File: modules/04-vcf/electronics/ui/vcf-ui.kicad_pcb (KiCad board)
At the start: 2 copper layers, 58 x 110 mm, 46 parts, among them J1 Conn_02x03_Odd_Even, J2 Conn_02x02_Counter_Clockwise, J4 Conn_01x02, J5 Conn_01x06, J6 Conn_02x04_Odd_Even, U1 TL072

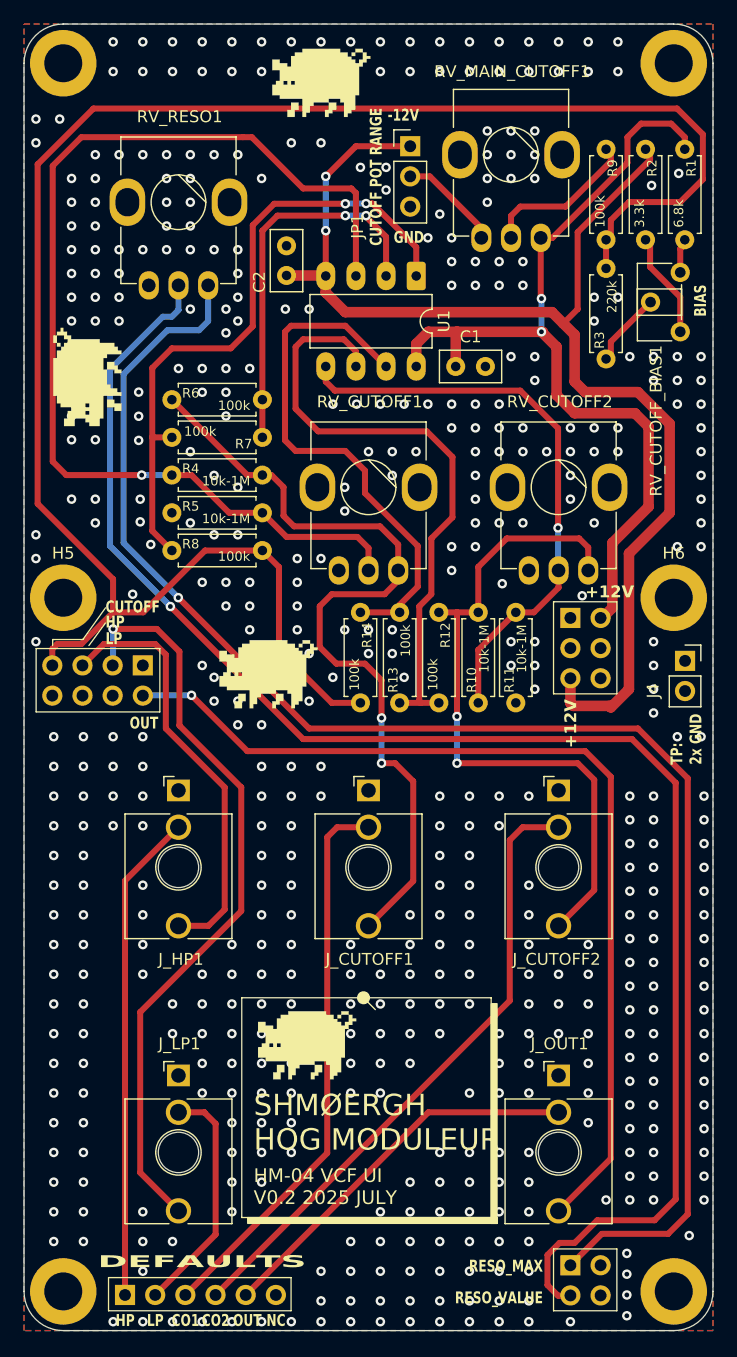
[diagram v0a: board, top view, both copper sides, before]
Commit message: Fixed VCF connector positions
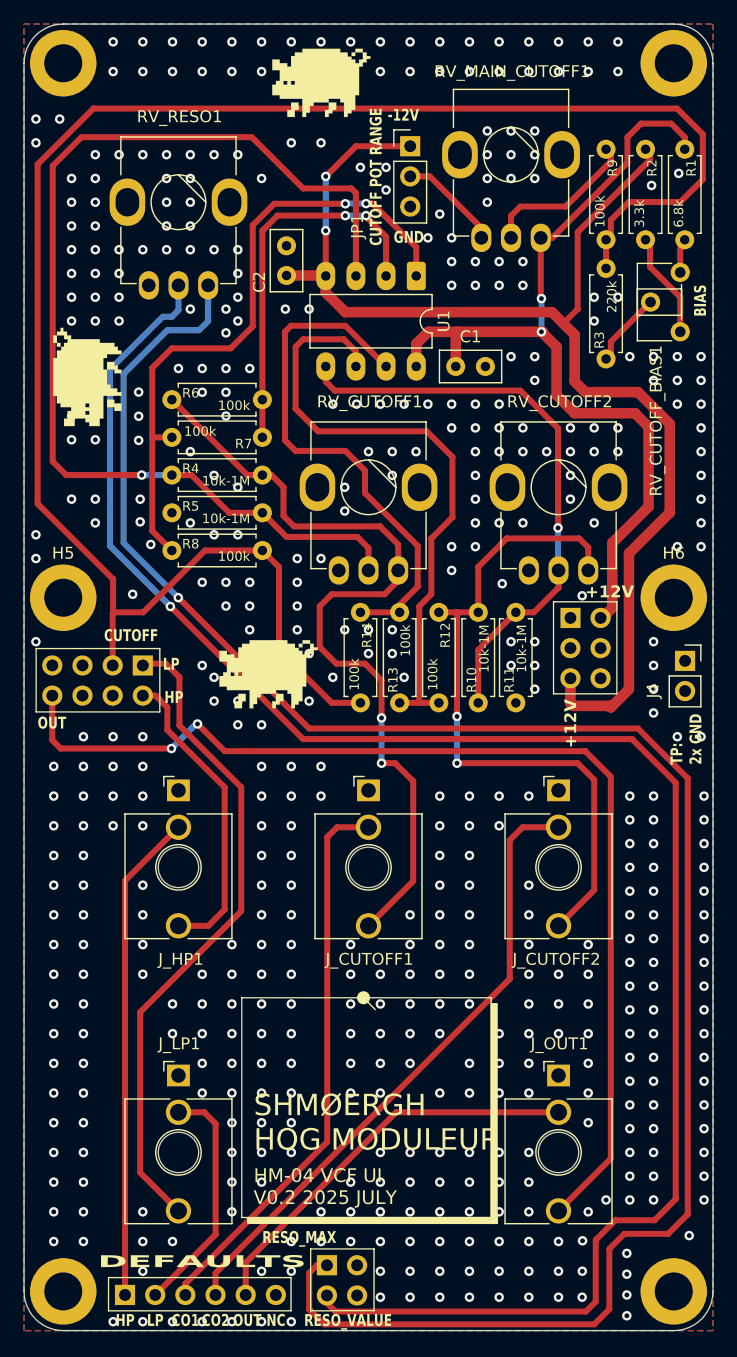
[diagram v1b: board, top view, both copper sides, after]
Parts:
- removed the G*** at (147.8, 130.0)
- C1, C2: value C -> 100n
- moved J2 20.5 mm to (149.5, 148.5)
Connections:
- J6 pad 1: unconnected-(J6-Pin_1-Pad1) -> LP_IN
- J6 pad 2: OUT -> HP_IN
- J6 pad 3: LP_IN -> CUTOFF
- J6 pad 5: HP_IN -> unconnected-(J6-Pin_5-Pad5)
- J6 pad 7: CUTOFF -> unconnected-(J6-Pin_7-Pad7)
- J6 pad 8: unconnected-(J6-Pin_8-Pad8) -> OUT
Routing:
- net RESO_MAX: track 130.3 -> 162.6 mm
- net RESO_VALUE: track 133.3 -> 153.0 mm
- net OUT: track 80.6 -> 92.1 mm, vias 1 -> 2
- net HP_IN: track 36.1 -> 26.0 mm
- net LP_IN: track 63.6 -> 55.6 mm, vias 1 -> 0
- net CUTOFF: track 156.6 -> 153.3 mm
- net OUT_DEFAULT: track 32.7 -> 34.3 mm
- net GND: vias 523 -> 528

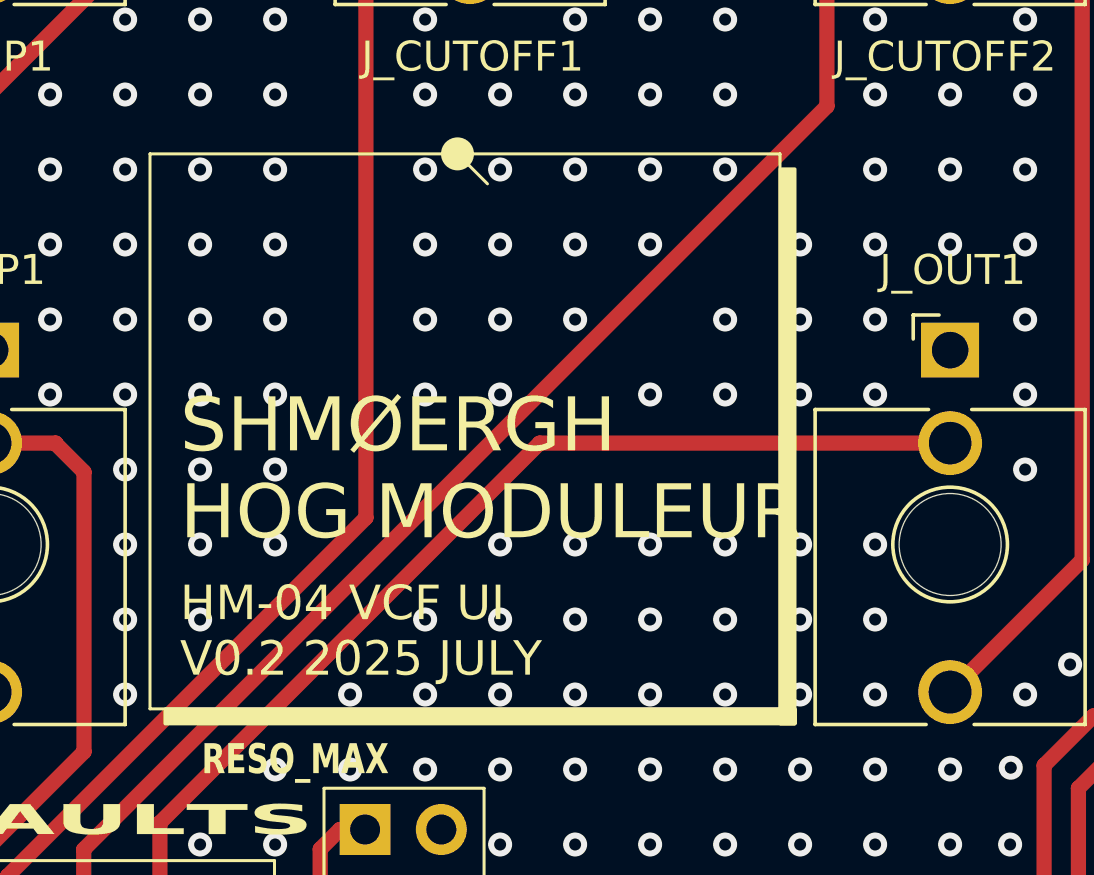
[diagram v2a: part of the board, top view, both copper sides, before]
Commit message: Updated text on PCB
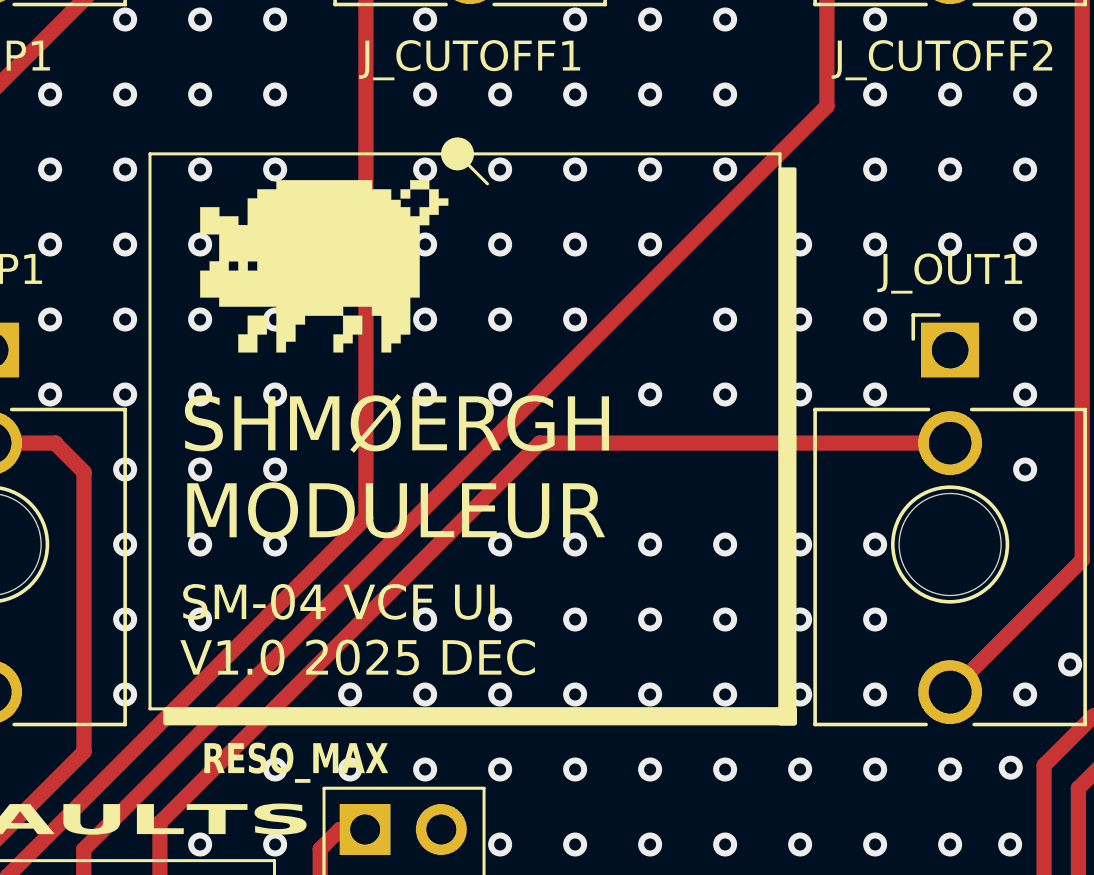
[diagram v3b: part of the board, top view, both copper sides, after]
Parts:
- added G***: LOGO, Shmoergh_Logo:Gyeszno, F.Cu at (148.1, 129.7)
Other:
- board text added: "SHMØERGH MODULEUR"
- board text added: "SM-04 VCF UI V1.0 2025 DEC"
- board text removed: "HM-04 VCF UI V0.2 2025 JULY"
- board text removed: "SHMØERGH HOG MODULEUR"

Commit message: KiCAD version update - VCF
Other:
- board text added: "SM-04 VCF UI V1.0"
- board text removed: "SM-04 VCF UI V1.0 2025 DEC"
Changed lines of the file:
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@@
 		)
 	)
-	(gr_text "SM-04 VCF UI \nV1.0 2025 DEC"
+	(gr_text "SM-04 VCF UI \nV1.0"
 		(at 143.329 143.479 0)
 		(layer "F.SilkS")
@@
 			(justify left bottom)
 		)
-		(render_cache "SM-04 VCF UI \nV1.0 2025 DEC" 0
+		(render_cache "SM-04 VCF UI \nV1.0" 0
 			(polygon
 				(pts
@@
 				)
 			)
-			(polygon
-				(pts
-					(xy 148.592958 142.990823) (xy 148.592958 143.2835) (xy 149.324789 143.2835) (xy 149.324789 143.137161)
-					(xy 148.739296 143.137161) (xy 148.739296 142.990823)
-				)
-			)
-			(polygon
-				(pts
-					(xy 149.178381 142.258992) (xy 149.178381 142.112584) (xy 148.739296 142.112584) (xy 148.739296 142.258992)
-				)
-			)
-			(polygon
-				(pts
-					(xy 149.178381 142.258992) (xy 149.178381 142.551739) (xy 149.324789 142.551739) (xy 149.324789 142.258992)
-				)
-			)
-			(polygon
-				(pts
-					(xy 148.739296 142.844415) (xy 148.739296 142.990823) (xy 148.885704 142.990823) (xy 148.885704 142.844415)
-				)
-			)
-			(polygon
-				(pts
-					(xy 148.592958 142.258992) (xy 148.592958 142.40533) (xy 148.739296 142.40533) (xy 148.739296 142.258992)
-				)
-			)
-			(polygon
-				(pts
-					(xy 149.032043 142.551739) (xy 149.032043 142.698077) (xy 149.178381 142.698077) (xy 149.178381 142.551739)
-				)
-			)
-			(polygon
-				(pts
-					(xy 148.885704 142.698077) (xy 148.885704 142.844415) (xy 149.032043 142.844415) (xy 149.032043 142.698077)
-				)
-			)
-			(polygon
-				(pts
-					(xy 149.616482 142.258992) (xy 149.616482 143.137161) (xy 149.76282 143.137161) (xy 149.76282 142.844415)
-					(xy 149.909228 142.844415) (xy 149.909228 142.698077) (xy 149.76282 142.698077) (xy 149.76282 142.258992)
-				)
-			)
-			(polygon
-				(pts
-					(xy 149.76282 143.137161) (xy 149.76282 143.2835) (xy 150.201905 143.2835) (xy 150.201905 143.137161)
-				)
-			)
-			(polygon
-				(pts
-					(xy 149.76282 142.112584) (xy 149.76282 142.258992) (xy 150.201905 142.258992) (xy 150.201905 142.112584)
-				)
-			)
-			(polygon
-				(pts
-					(xy 150.201905 142.258992) (xy 150.201905 142.40533) (xy 150.055567 142.40533) (xy 150.055567 142.551739)
-					(xy 150.201905 142.551739) (xy 150.201905 143.137161) (xy 150.348313 143.137161) (xy 150.348313 142.258992)
-				)
-			)
-			(polygon
-				(pts
-					(xy 149.909228 142.551739) (xy 149.909228 142.698077) (xy 150.055567 142.698077) (xy 150.055567 142.551739)
-				)
-			)
-			(polygon
-				(pts
-					(xy 150.640006 142.990823) (xy 150.640006 143.2835) (xy 151.371837 143.2835) (xy 151.371837 143.137161)
-					(xy 150.786344 143.137161) (xy 150.786344 142.990823)
-				)
-			)
-			(polygon
-				(pts
-					(xy 151.225429 142.258992) (xy 151.225429 142.112584) (xy 150.786344 142.112584) (xy 150.786344 142.258992)
-				)
-			)
-			(polygon
-				(pts
-					(xy 151.225429 142.258992) (xy 151.225429 142.551739) (xy 151.371837 142.551739) (xy 151.371837 142.258992)
-				)
-			)
-			(polygon
-				(pts
-					(xy 150.786344 142.844415) (xy 150.786344 142.990823) (xy 150.932753 142.990823) (xy 150.932753 142.844415)
-				)
-			)
-			(polygon
-				(pts
-					(xy 150.640006 142.258992) (xy 150.640006 142.40533) (xy 150.786344 142.40533) (xy 150.786344 142.258992)
-				)
-			)
-			(polygon
-				(pts
-					(xy 151.079091 142.551739) (xy 151.079091 142.698077) (xy 151.225429 142.698077) (xy 151.225429 142.551739)
-				)
-			)
-			(polygon
-				(pts
-					(xy 150.932753 142.698077) (xy 150.932753 142.844415) (xy 151.079091 142.844415) (xy 151.079091 142.698077)
-				)
-			)
-			(polygon
-				(pts
-					(xy 151.66353 142.112584) (xy 151.66353 142.698077) (xy 152.248953 142.698077) (xy 152.248953 142.551739)
-					(xy 151.809868 142.551739) (xy 151.809868 142.258992) (xy 152.395361 142.258992) (xy 152.395361 142.112584)
-				)
-			)
-			(polygon
-				(pts
-					(xy 152.248953 142.698077) (xy 152.248953 143.137161) (xy 152.395361 143.137161) (xy 152.395361 142.698077)
-				)
-			)
-			(polygon
-				(pts
-					(xy 152.248953 143.137161) (xy 151.809868 143.137161) (xy 151.809868 143.2835) (xy 152.248953 143.2835)
-				)
-			)
-			(polygon
-				(pts
-					(xy 151.809868 143.137161) (xy 151.809868 142.990823) (xy 151.66353 142.990823) (xy 151.66353 143.137161)
-				)
-			)
-			(polygon
-				(pts
-					(xy 153.710578 142.112584) (xy 153.710578 143.2835) (xy 154.296001 143.2835) (xy 154.296001 143.137161)
-					(xy 153.856916 143.137161) (xy 153.856916 142.258992) (xy 154.296001 142.258992) (xy 154.296001 142.112584)
-				)
-			)
-			(polygon
-				(pts
-					(xy 154.296001 142.258992) (xy 154.296001 143.137161) (xy 154.442409 143.137161) (xy 154.442409 142.258992)
-				)
-			)
-			(polygon
-				(pts
-					(xy 154.734102 142.112584) (xy 154.734102 143.2835) (xy 155.465933 143.2835) (xy 155.465933 143.137161)
-					(xy 154.880441 143.137161) (xy 154.880441 142.698077) (xy 155.319525 142.698077) (xy 155.319525 142.551739)
-					(xy 154.880441 142.551739) (xy 154.880441 142.258992) (xy 155.465933 142.258992) (xy 155.465933 142.112584)
-				)
-			)
-			(polygon
-				(pts
-					(xy 155.757627 142.258992) (xy 155.757627 143.137161) (xy 155.903965 143.137161) (xy 155.903965 142.258992)
-				)
-			)
-			(polygon
-				(pts
-					(xy 155.903965 143.137161) (xy 155.903965 143.2835) (xy 156.343049 143.2835) (xy 156.343049 143.137161)
-				)
-			)
-			(polygon
-				(pts
-					(xy 156.343049 142.990823) (xy 156.343049 143.137161) (xy 156.489457 143.137161) (xy 156.489457 142.990823)
-				)
-			)
-			(polygon
-				(pts
-					(xy 155.903965 142.112584) (xy 155.903965 142.258992) (xy 156.343049 142.258992) (xy 156.343049 142.112584)
-				)
-			)
-			(polygon
-				(pts
-					(xy 156.343049 142.258992) (xy 156.343049 142.40533) (xy 156.489457 142.40533) (xy 156.489457 142.258992)
-				)
-			)

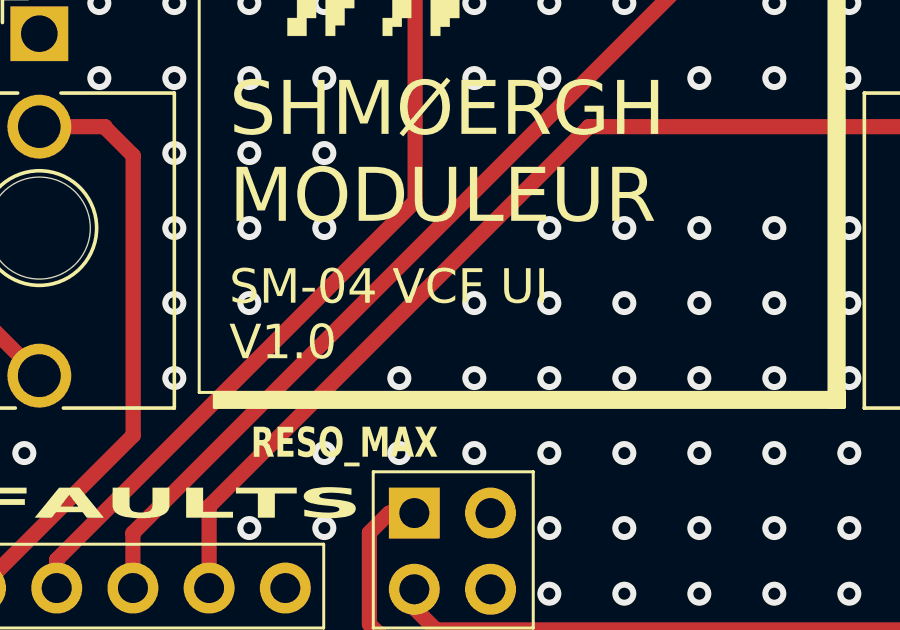
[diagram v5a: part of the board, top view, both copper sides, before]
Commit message: Changed board versioning to 'rev' on VCF
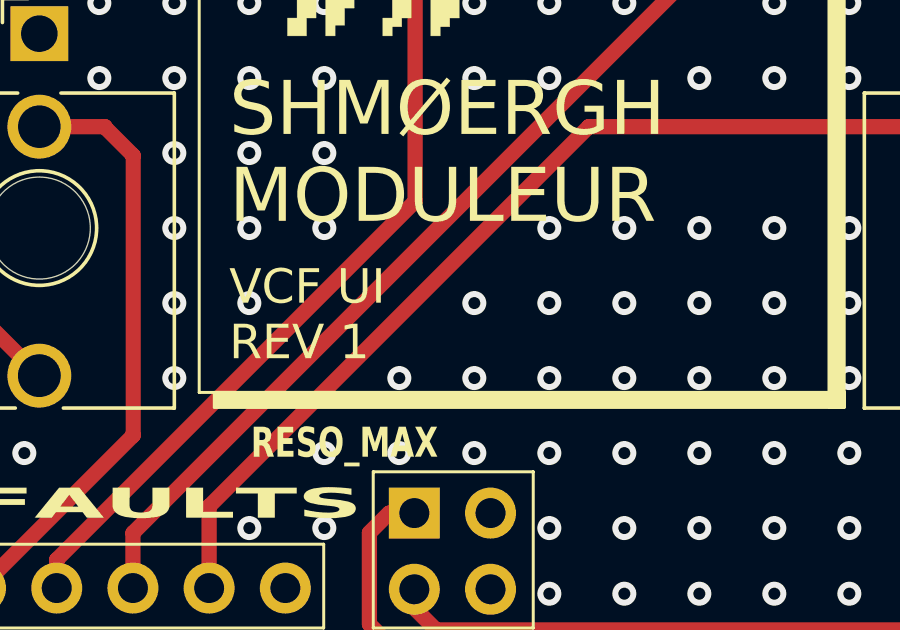
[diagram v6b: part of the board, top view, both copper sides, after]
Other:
- board text added: "VCF UI REV 1"
- board text removed: "SM-04 VCF UI V1.0"

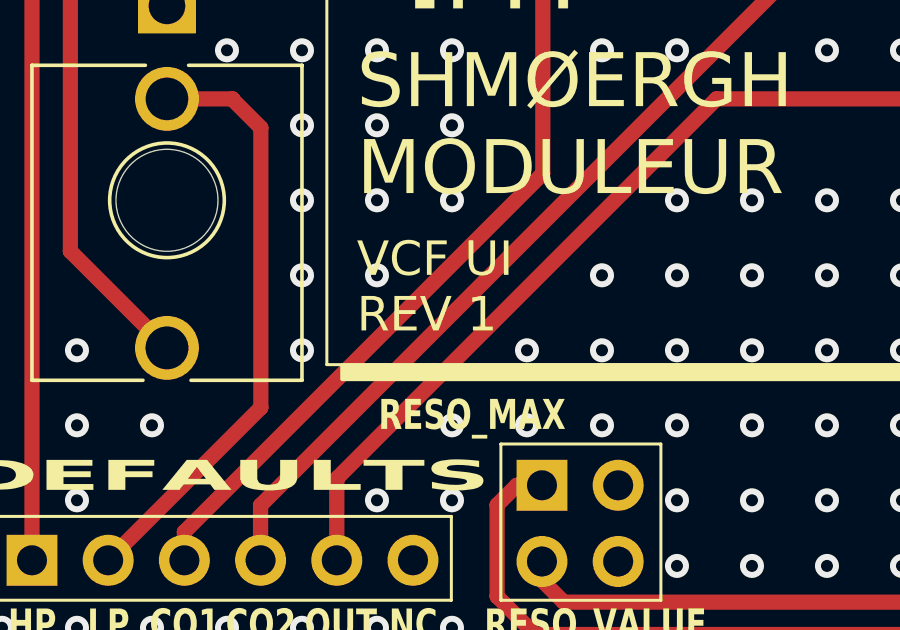
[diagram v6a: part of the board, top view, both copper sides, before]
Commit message: Fixed VCF UI schemo and PCB after fckckin KiCAD update
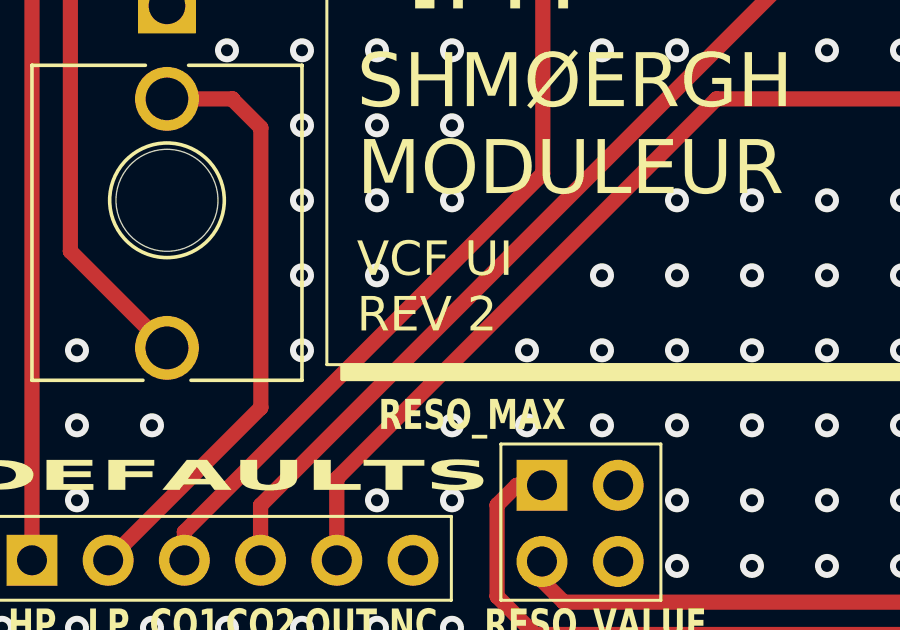
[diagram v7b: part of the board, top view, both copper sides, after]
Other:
- board text added: "VCF UI REV 2"
- board text removed: "VCF UI REV 1"
